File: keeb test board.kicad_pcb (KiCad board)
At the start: 2 copper layers, 60 x 100 mm, 63 parts, among them SW1 SW_Push, SW10 SW_Push, SW11 SW_Push, SW12 SW_Push, SW13 SW_Push, SW14 SW_Push, SW15 SW_Push, SW2 SW_Push, SW3 SW_Push, SW4 SW_Push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

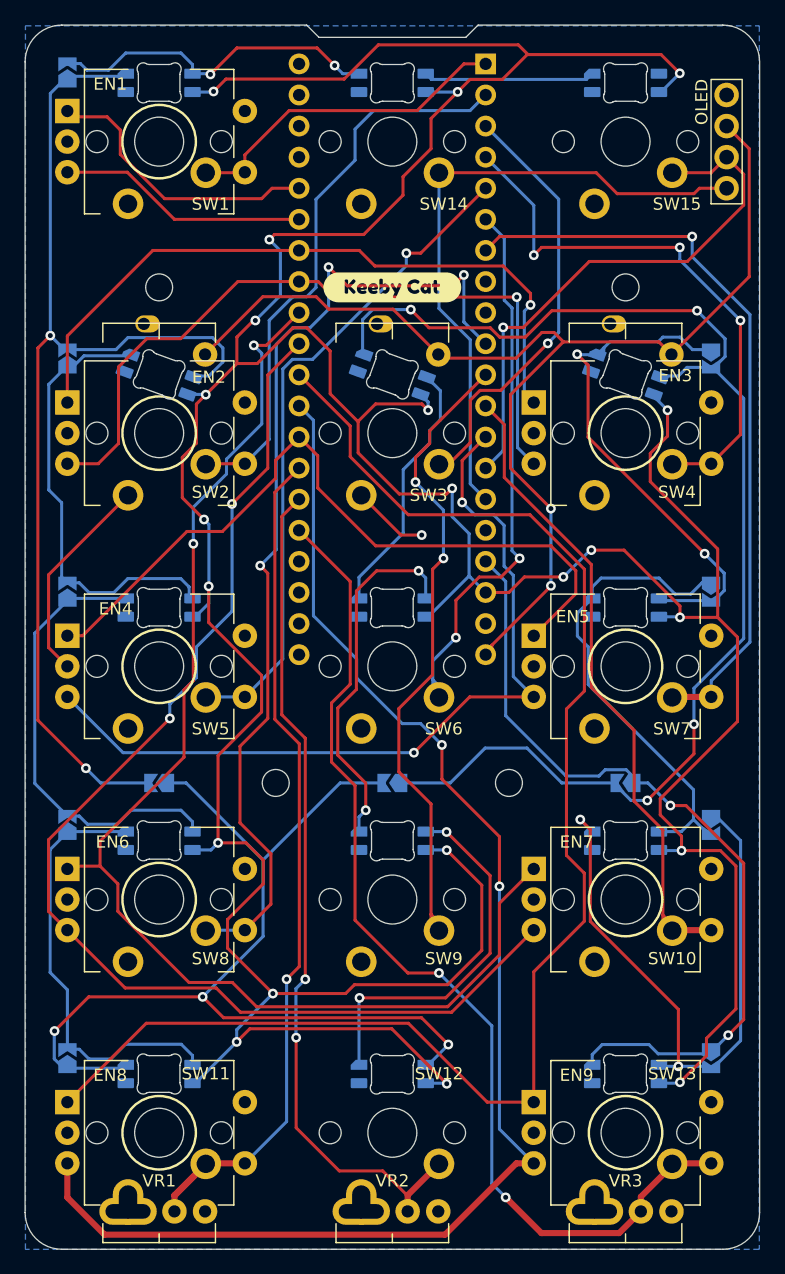
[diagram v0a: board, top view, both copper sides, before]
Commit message: improved thin spots in ground plane, removed via
also very small routing improvements
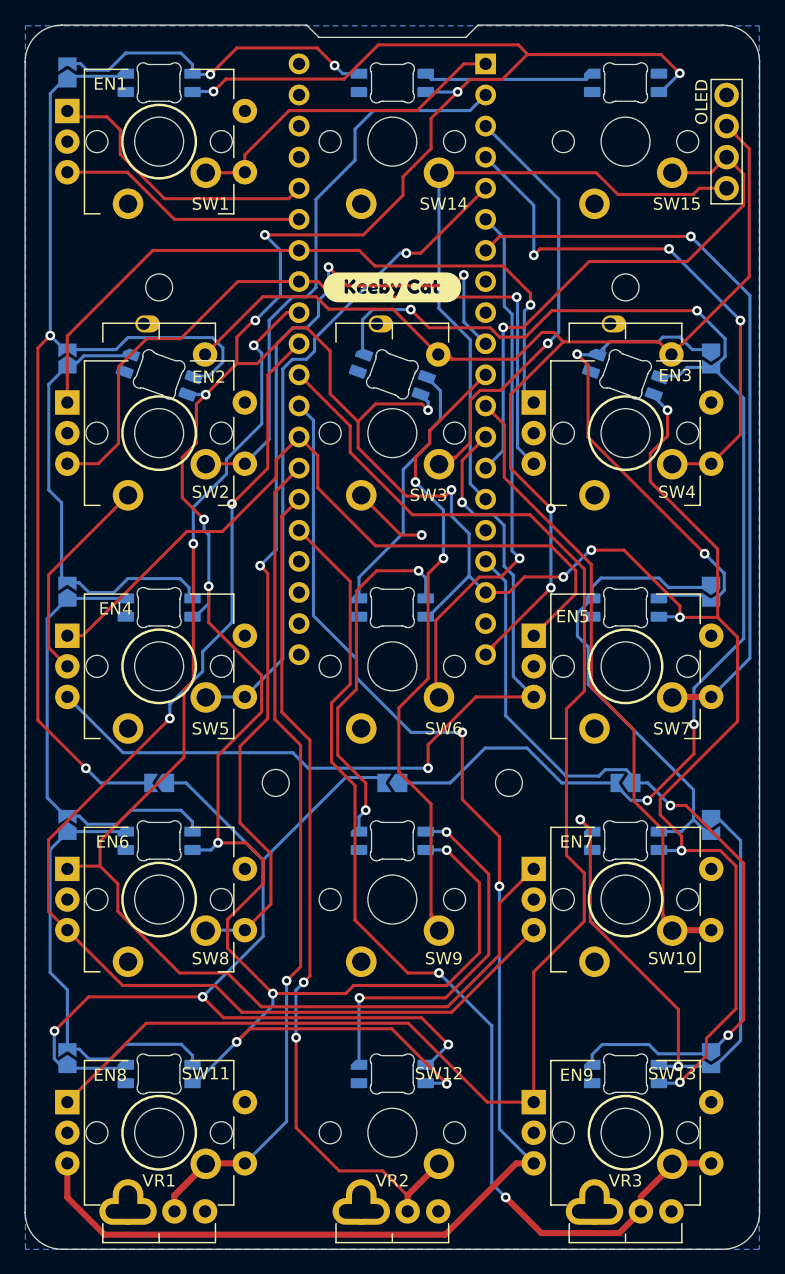
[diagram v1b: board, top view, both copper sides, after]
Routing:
- net ENC3B: track 67.2 -> 69.4 mm
- net +3V3: track 97.3 -> 99.3 mm
- net ENC5B: track 115.2 -> 116.8 mm
- net KEY6: track 45.3 -> 44.2 mm, vias 2 -> 1
- net KEY3: track 35.6 -> 36.5 mm
- net KEY4: track 45.7 -> 45.0 mm
- net Net-(D10-Pad2): track 36.8 -> 36.2 mm

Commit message: LED pins fixed, lots of rerouting
Corrected LED and routed accordingly. Lots of other misc, changes to improve routing.
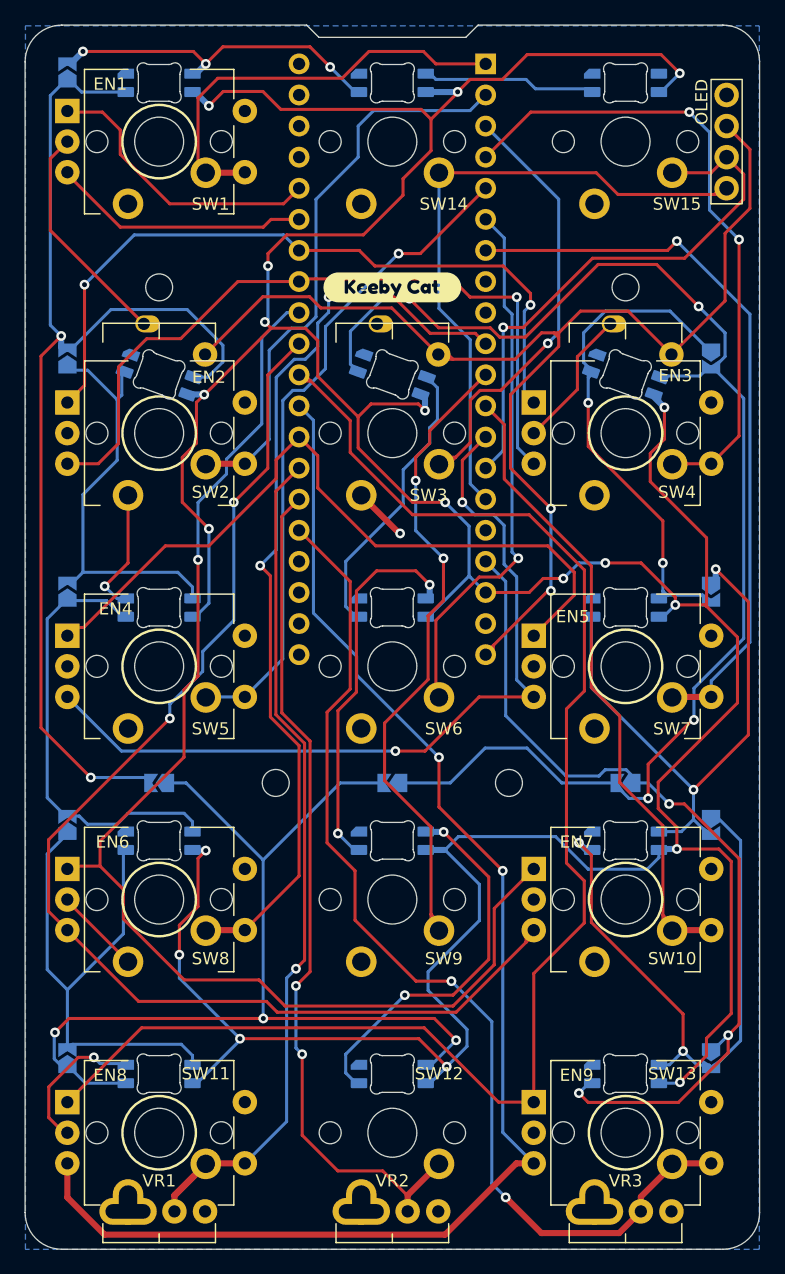
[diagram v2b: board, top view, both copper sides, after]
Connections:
- VR1 pad 3: unconnected-(VR1-Pad3) -> GND
- VR2 pad 3: unconnected-(VR2-Pad3) -> GND
- VR3 pad 3: unconnected-(VR3-Pad3) -> GND
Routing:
- net GND: track 23.6 -> 64.2 mm, vias 1 -> 3
- net +5V: track 369.1 -> 335.6 mm, vias 21 -> 19
- net Net-(D2-Pad2): track 39.1 -> 47.5 mm, vias 0 -> 2
- net Net-(D10-Pad4): track 35.9 -> 43.9 mm
- net KEY1: track 27.3 -> 35.0 mm
- net KEY4: track 45.0 -> 52.7 mm, vias 3 -> 2
- net KEY8: track 81.9 -> 75.3 mm, vias 3 -> 2
- net Net-(D4-Pad2): track 106.0 -> 112.1 mm
- net LED_DATA: track 65.8 -> 71.1 mm, vias 2 -> 3
- net +3V3: track 99.3 -> 102.0 mm
- net Net-(D12-Pad2): track 89.1 -> 91.8 mm
- net ENC2A: track 57.1 -> 59.7 mm, vias 1 -> 2
- net ENC5B: track 116.8 -> 114.4 mm
- net Net-(D5-Pad2): track 21.3 -> 23.6 mm
- net ENC3B: track 69.4 -> 67.1 mm
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
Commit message: minor routing tweaks
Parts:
- moved kibuzzard-6227022E 0.86 mm to (92.2, 77.6)
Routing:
- net +5V: track 335.6 -> 332.3 mm
- net GND: track 64.2 -> 66.0 mm
- net ENC2A: track 59.7 -> 58.8 mm

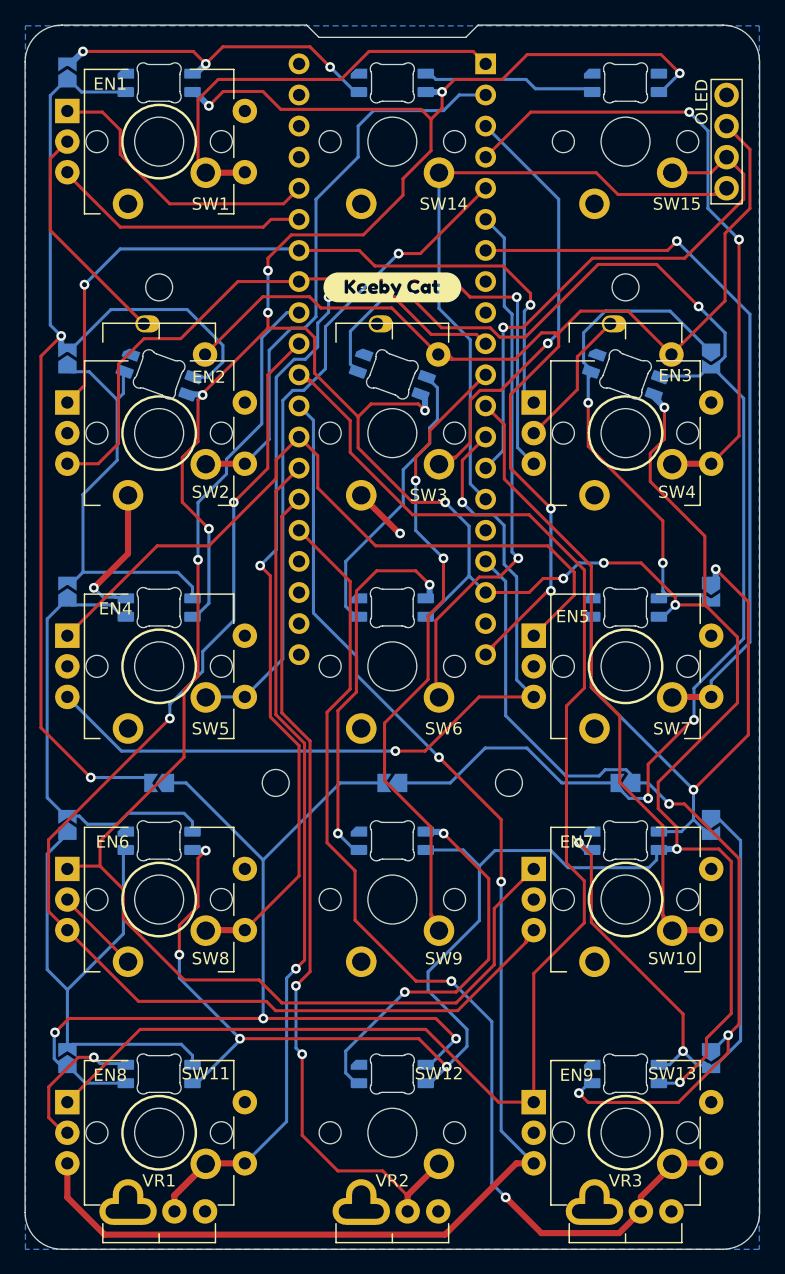
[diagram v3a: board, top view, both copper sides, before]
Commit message: adjusted silkscreen
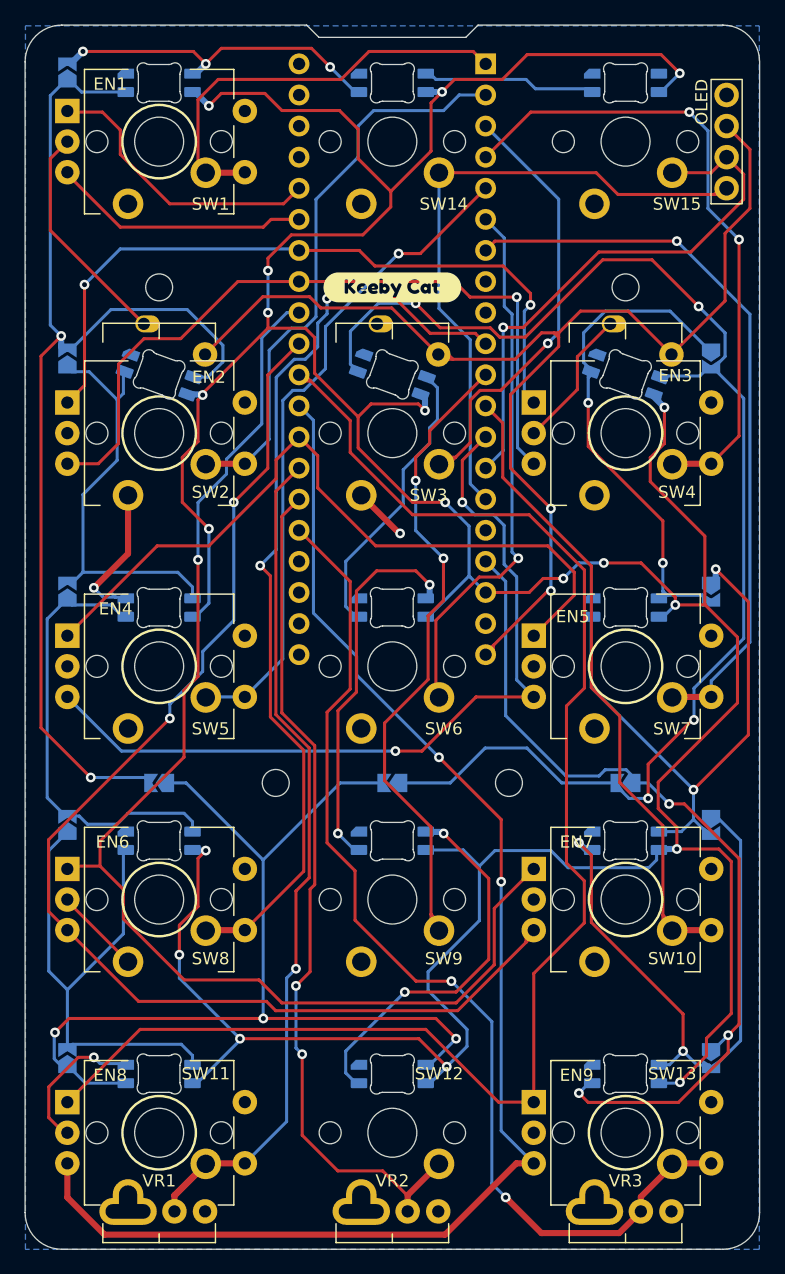
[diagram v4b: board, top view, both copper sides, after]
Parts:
- moved kibuzzard-6226FF10 1.27 mm to (109.6, 136.9)
